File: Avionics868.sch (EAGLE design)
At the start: 65 parts, among them SW1 B3U-1000P-2P-SMD, U1 ATSAMD21G18_QFN, U2 SPX3819M5-L-3-0, U3 MCP73831T-2ACI/OT, U4 MPU-9250, U5 SIM868, U6 BMP180, X1 JSTPH, X2 32.768, X3 microUSB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

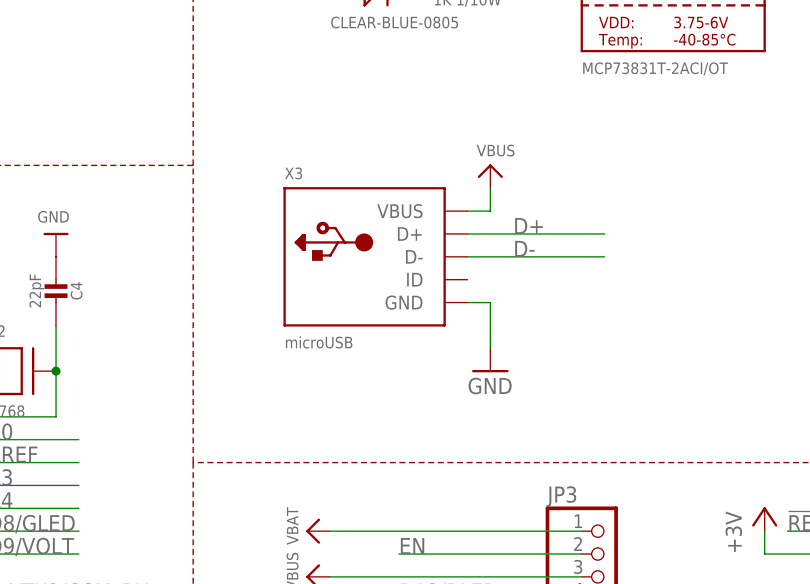
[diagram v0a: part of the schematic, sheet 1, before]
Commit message: Swapped Micro-USB connector for Seeed
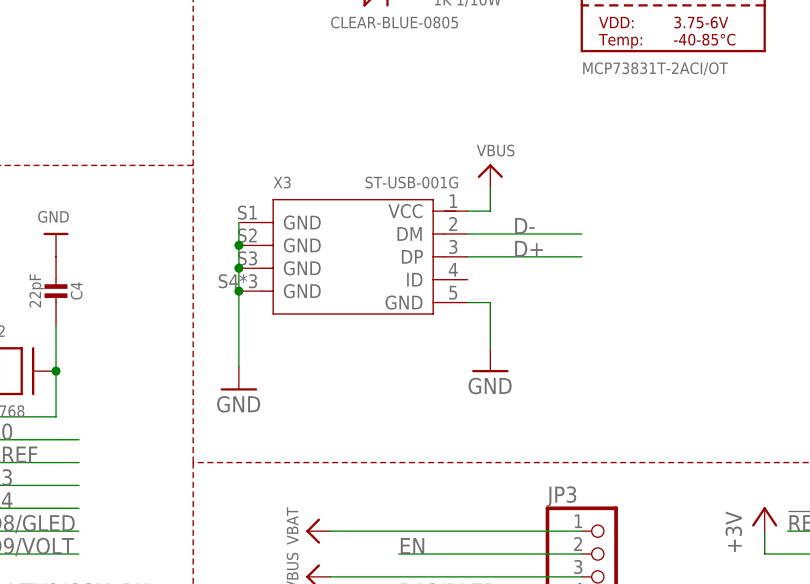
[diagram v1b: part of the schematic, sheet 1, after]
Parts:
- X3: value microUSB -> ST-USB-001G; device microbuilder:USB_MICRO_20329_V2 -> Seeed-Connector -2016:MICRO-USB-SMD-B-WITHOUT-POST-W/P(ST-USB-001G)
- renumbered X6 to X4
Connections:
- net D+: now also X3.DP; no longer X3.D+
- net D-: now also X3.DM; no longer X3.D-
- net GND: now also X3.GND@1, X3.GND@2, X3.GND@3, X3.GND@4, X3.GND@5; no longer X3.GND
- net VBUS: now also X3.VCC; no longer X3.VBUS
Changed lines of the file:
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@@
 <part name="U$3" library="microbuilder" deviceset="VBUS" device=""/>
 <part name="U$21" library="microbuilder" deviceset="VBAT" device=""/>
-<part name="X3" library="microbuilder" deviceset="USB" device="_MICRO_20329_V2" value="microUSB"/>
 <part name="U2" library="microbuilder" deviceset="VREG_SOT23-5" device="" value="SPX3819M5-L-3-0"/>
 <part name="D1" library="microbuilder" deviceset="DIODE-SCHOTTKY" device="SOD-123" value="MBR120"/>
@@
 <part name="U$47" library="microbuilder" deviceset="VBAT" device=""/>
 <part name="TP13" library="microbuilder" deviceset="TESTPOINT" device="ROUND1.5MM"/>
-<part name="X6" library="SimSdCombo" deviceset="MOLEX-SD+SIM-104239" device="" value="VSHO-21-3301"/>
+<part name="X4" library="SimSdCombo" deviceset="MOLEX-SD+SIM-104239" device="" value="VSHO-21-3301"/>
 <part name="U$4" library="microbuilder" deviceset="GND" device=""/>
 <part name="+3V11" library="Custom" deviceset="+3V" device=""/>
@@
 <part name="U$51" library="microbuilder" deviceset="GND" device=""/>
 <part name="SW1" library="Seeed-Switch-2016" deviceset="SMD-BUTTON(2P-3.0X2.5X1.2+0.4MM)" device="-B3U-1000P-2P-SMD" value="B3U-1000P-2P-SMD"/>
+<part name="X3" library="Seeed-Connector -2016" deviceset="MICRO-USB-SMD-B-WITHOUT-POST-W/P(ST-USB-001G)" device="" value="ST-USB-001G"/>
+<part name="GND2" library="supply1" deviceset="GND" device=""/>
 </parts>
 <sheets>
@@
 <instance part="U$3" gate="G$1" x="7.62" y="160.02"/>
 <instance part="U$21" gate="G$1" x="12.7" y="160.02"/>
-<instance part="X3" gate="G$1" x="154.94" y="111.76"/>
 <instance part="U2" gate="G$1" x="38.1" y="144.78"/>
 <instance part="D1" gate="G$1" x="12.7" y="154.94" rot="R270"/>
@@
 <attribute name="VALUE" x="113.538" y="160.274" size="1.27" layer="96" ratio="10"/>
 </instance>
+<instance part="X3" gate="USB" x="152.4" y="111.76"/>
+<instance part="GND2" gate="1" x="139.7" y="97.028"/>
 </instances>
 <busses>
@@
 <wire x1="167.64" y1="106.68" x2="167.64" y2="101.6" width="0.1524" layer="91"/>
 <pinref part="GND1" gate="1" pin="GND"/>
-<pinref part="X3" gate="G$1" pin="GND"/>
+<pinref part="X3" gate="USB" pin="GND@5"/>
 </segment>
 <segment>
@@
 <pinref part="GND9" gate="1" pin="GND"/>
 <wire x1="236.22" y1="46.99" x2="236.22" y2="45.72" width="0.1524" layer="91"/>
+</segment>
+<segment>
+<pinref part="X3" gate="USB" pin="GND@1"/>
+<wire x1="139.7" y1="115.57" x2="139.7" y2="113.03" width="0.1524" layer="91"/>
+<pinref part="GND2" gate="1" pin="GND"/>
+<pinref part="X3" gate="USB" pin="GND@2"/>
+<junction x="139.7" y="113.03"/>
+<wire x1="139.7" y1="113.03" x2="139.7" y2="110.49" width="0.1524" layer="91"/>
+<pinref part="X3" gate="USB" pin="GND@3"/>
+<junction x="139.7" y="110.49"/>
+<wire x1="139.7" y1="110.49" x2="139.7" y2="107.95" width="0.1524" layer="91"/>
+<pinref part="X3" gate="USB" pin="GND@4"/>
+<junction x="139.7" y="107.95"/>
+<wire x1="139.7" y1="107.95" x2="139.7" y2="99.568" width="0.1524" layer="91"/>
 </segment>
 </net>
@@
 <wire x1="167.64" y1="116.84" x2="167.64" y2="119.38" width="0.1524" layer="91"/>
 <pinref part="U$1" gate="G$1" pin="VBUS"/>
-<pinref part="X3" gate="G$1" pin="VBUS"/>
+<pinref part="X3" gate="USB" pin="VCC"/>
 </segment>
 <segment>
@@
 <net name="D+" class="0">
 <segment>
-<pinref part="X3" gate="G$1" pin="D+"/>
-<wire x1="165.1" y1="114.3" x2="180.34" y2="114.3" width="0.1524" layer="91"/>
-<label x="170.18" y="114.3" size="1.778" layer="95"/>
+<wire x1="165.1" y1="111.76" x2="177.8" y2="111.76" width="0.1524" layer="91"/>
+<label x="170.18" y="111.76" size="1.778" layer="95"/>
+<pinref part="X3" gate="USB" pin="DP"/>
 </segment>
 <segment>
@@
 <net name="D-" class="0">
 <segment>
-<pinref part="X3" gate="G$1" pin="D-"/>
-<wire x1="180.34" y1="111.76" x2="165.1" y2="111.76" width="0.1524" layer="91"/>
-<label x="170.18" y="111.76" size="1.778" layer="95"/>
+<wire x1="177.8" y1="114.3" x2="165.1" y2="114.3" width="0.1524" layer="91"/>
+<label x="170.18" y="114.3" size="1.778" layer="95"/>
+<pinref part="X3" gate="USB" pin="DM"/>
 </segment>
 <segment>
@@
 <attribute name="VALUE" x="134.112" y="98.171" size="1.27" layer="95" rot="R180" align="center-left"/>
 </instance>
-<instance part="X6" gate="G$1" x="106.68" y="86.36"/>
+<instance part="X4" gate="G$1" x="106.68" y="86.36"/>
 <instance part="U$4" gate="G$1" x="68.58" y="86.36" smashed="yes">
 <attribute name="VALUE" x="64.516" y="87.63" size="1.27" layer="96"/>
@@
 </segment>
 <segment>
-<pinref part="X6" gate="G$1" pin="GND@8"/>
-<pinref part="X6" gate="G$1" pin="GND@1"/>
+<pinref part="X4" gate="G$1" pin="GND@8"/>
+<pinref part="X4" gate="G$1" pin="GND@1"/>
 <wire x1="114.3" y1="68.58" x2="111.76" y2="68.58" width="0.1524" layer="91"/>
-<pinref part="X6" gate="G$1" pin="GND@2"/>
+<pinref part="X4" gate="G$1" pin="GND@2"/>
 <junction x="99.06" y="68.58"/>
 <wire x1="111.76" y1="68.58" x2="109.22" y2="68.58" width="0.1524" layer="91"/>
@@
 <wire x1="101.6" y1="68.58" x2="99.06" y2="68.58" width="0.1524" layer="91"/>
 <wire x1="99.06" y1="68.58" x2="96.52" y2="68.58" width="0.1524" layer="91"/>
-<pinref part="X6" gate="G$1" pin="GND@3"/>
+<pinref part="X4" gate="G$1" pin="GND@3"/>
 <junction x="101.6" y="68.58"/>
-<pinref part="X6" gate="G$1" pin="GND@4"/>
+<pinref part="X4" gate="G$1" pin="GND@4"/>
 <junction x="104.14" y="68.58"/>
-<pinref part="X6" gate="G$1" pin="GND@5"/>
+<pinref part="X4" gate="G$1" pin="GND@5"/>
 <junction x="106.68" y="68.58"/>
-<pinref part="X6" gate="G$1" pin="GND@6"/>
+<pinref part="X4" gate="G$1" pin="GND@6"/>
 <junction x="109.22" y="68.58"/>
-<pinref part="X6" gate="G$1" pin="GND@7"/>
+<pinref part="X4" gate="G$1" pin="GND@7"/>
 <junction x="111.76" y="68.58"/>
 <pinref part="U$43" gate="G$1" pin="GND"/>
@@
 </segment>
 <segment>
-<pinref part="X6" gate="G$1" pin="SIM_GND"/>
+<pinref part="X4" gate="G$1" pin="SIM_GND"/>
 <pinref part="U$48" gate="G$1" pin="GND"/>
 <wire x1="119.38" y1="111.76" x2="119.38" y2="119.38" width="0.1524" layer="91"/>
@@
 </segment>
 <segment>
-<pinref part="X6" gate="G$1" pin="SD_VSS"/>
+<pinref part="X4" gate="G$1" pin="SD_VSS"/>
 <pinref part="U$4" gate="G$1" pin="GND"/>
 <wire x1="91.44" y1="91.44" x2="68.58" y2="91.44" width="0.1524" layer="91"/>
@@
 </segment>
 <segment>
-<pinref part="X6" gate="G$1" pin="SD_VDD"/>
+<pinref part="X4" gate="G$1" pin="SD_VDD"/>
 <pinref part="+3V11" gate="G$1" pin="+3V"/>
 <wire x1="91.44" y1="96.52" x2="68.58" y2="96.52" width="0.1524" layer="91"/>
@@
 </segment>
 <segment>
-<pinref part="X6" gate="G$1" pin="SIM_VCC"/>
+<pinref part="X4" gate="G$1" pin="SIM_VCC"/>
 <wire x1="111.76" y1="111.76" x2="111.76" y2="114.3" width="0.1524" layer="91"/>
 <wire x1="111.76" y1="114.3" x2="93.98" y2="114.3" width="0.1524" layer="91"/>
@@
 </segment>
 <segment>
-<pinref part="X6" gate="G$1" pin="SIM_I/O"/>
+<pinref part="X4" gate="G$1" pin="SIM_I/O"/>
 <wire x1="124.46" y1="111.76" x2="124.46" y2="121.92" width="0.1524" layer="91"/>
 <wire x1="124.46" y1="121.92" x2="93.98" y2="121.92" width="0.1524" layer="91"/>
@@
 </segment>
 <segment>
-<pinref part="X6" gate="G$1" pin="SIM_CLK"/>
+<pinref part="X4" gate="G$1" pin="SIM_CLK"/>
 <wire x1="116.84" y1="111.76" x2="116.84" y2="119.38" width="0.1524" layer="91"/>
 <wire x1="116.84" y1="119.38" x2="93.98" y2="119.38" width="0.1524" layer="91"/>
@@
 </segment>
 <segment>
-<pinref part="X6" gate="G$1" pin="SIM_RST"/>
+<pinref part="X4" gate="G$1" pin="SIM_RST"/>
 <wire x1="114.3" y1="111.76" x2="114.3" y2="116.84" width="0.1524" layer="91"/>
 <wire x1="114.3" y1="116.84" x2="93.98" y2="116.84" width="0.1524" layer="91"/>
@@
 <net name="MOSI" class="0">
 <segment>
-<pinref part="X6" gate="G$1" pin="SD_CMD"/>
+<pinref part="X4" gate="G$1" pin="SD_CMD"/>
 <wire x1="91.44" y1="99.06" x2="73.66" y2="99.06" width="0.1524" layer="91"/>
 <label x="73.66" y="99.06" size="1.778" layer="95"/>
@@
 <net name="SCK" class="0">
 <segment>
-<pinref part="X6" gate="G$1" pin="SD_CLK"/>
+<pinref part="X4" gate="G$1" pin="SD_CLK"/>
 <wire x1="91.44" y1="93.98" x2="73.66" y2="93.98" width="0.1524" layer="91"/>
 <label x="73.66" y="93.98" size="1.778" layer="95"/>
@@
 <net name="D7/SD_CS" class="0">
 <segment>
-<pinref part="X6" gate="G$1" pin="SD_CD/DAT3"/>
+<pinref part="X4" gate="G$1" pin="SD_CD/DAT3"/>
 <wire x1="91.44" y1="101.6" x2="73.66" y2="101.6" width="0.1524" layer="91"/>
 <label x="73.66" y="101.6" size="1.778" layer="95"/>
@@
 <net name="MISO" class="0">
 <segment>
-<pinref part="X6" gate="G$1" pin="SD_DAT0"/>
+<pinref part="X4" gate="G$1" pin="SD_DAT0"/>
 <wire x1="91.44" y1="88.9" x2="73.66" y2="88.9" width="0.1524" layer="91"/>
 <label x="73.66" y="88.9" size="1.778" layer="95"/>
@@
 <net name="SD_DET" class="0">
 <segment>
-<pinref part="X6" gate="G$1" pin="SD_SWITCH"/>
+<pinref part="X4" gate="G$1" pin="SD_SWITCH"/>
 <wire x1="91.44" y1="83.82" x2="73.66" y2="83.82" width="0.1524" layer="91"/>
 <pinref part="TP3" gate="G$1" pin="P$1"/>

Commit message: Swapped some capacitors
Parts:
- C3, C5: value 10uF -> 10uf; device microbuilder:CAP_CERAMIC0805-NOOUTLINE -> Seeed-Capacitor-2016:CERAMIC-10UF-10V-10%-X5R(0603)
- X4: value VSHO-21-3301 -> 104239-1430
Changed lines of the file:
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@@
 <part name="L3" library="Seeed-LED-2016" deviceset="SMD-LED-CLEAR-BLUE(0805)" device="" value="CLEAR-BLUE-0805"/>
 <part name="R2" library="Seeed-Resistor-2016" deviceset="SMD-RES-1K-5%-1/10W(0603)" device="" value="1K 1/10W"/>
-<part name="C3" library="microbuilder" deviceset="CAP_CERAMIC" device="0805-NOOUTLINE" value="10uF"/>
+<part name="C3" library="Seeed-Capacitor-2016" deviceset="CERAMIC-10UF-10V-10%-X5R(0603)" device="" value="10uf"/>
 <part name="U$33" library="microbuilder" deviceset="GND" device=""/>
 <part name="R8" library="Seeed-Resistor-2016" deviceset="SMD-RES-10K-5%-1/10W(0603)" device="" value="10K 1/10W"/>
@@
 <part name="U$10" library="microbuilder" deviceset="GND" device=""/>
 <part name="X2" library="adafruit2" deviceset="XTAL" device="-3.2X1.5" value="32.768"/>
-<part name="C5" library="microbuilder" deviceset="CAP_CERAMIC" device="0805-NOOUTLINE" value="10uF"/>
+<part name="C5" library="Seeed-Capacitor-2016" deviceset="CERAMIC-10UF-10V-10%-X5R(0603)" device="" value="10uf"/>
 <part name="+3V2" library="Custom" deviceset="+3V" device=""/>
 <part name="U$11" library="microbuilder" deviceset="GND" device=""/>
@@
 <part name="U$47" library="microbuilder" deviceset="VBAT" device=""/>
 <part name="TP13" library="microbuilder" deviceset="TESTPOINT" device="ROUND1.5MM"/>
-<part name="X4" library="SimSdCombo" deviceset="MOLEX-SD+SIM-104239" device="" value="VSHO-21-3301"/>
+<part name="X4" library="SimSdCombo" deviceset="MOLEX-SD+SIM-104239" device="" value="104239-1430"/>
 <part name="U$4" library="microbuilder" deviceset="GND" device=""/>
 <part name="+3V11" library="Custom" deviceset="+3V" device=""/>
@@
 <instance part="L3" gate="G$1" x="154.94" y="142.24"/>
 <instance part="R2" gate="G$1" x="165.1" y="142.24"/>
-<instance part="C3" gate="G$1" x="220.98" y="139.7"/>
+<instance part="C3" gate="G$1" x="220.98" y="139.7" rot="R270"/>
 <instance part="U$33" gate="G$1" x="220.98" y="129.54"/>
 <instance part="R8" gate="G$1" x="210.82" y="144.78"/>
@@
 <instance part="U$10" gate="G$1" x="119.38" y="114.3" rot="R180"/>
 <instance part="X2" gate="G$1" x="114.3" y="99.06"/>
-<instance part="C5" gate="G$1" x="93.98" y="137.16"/>
+<instance part="C5" gate="G$1" x="93.98" y="139.7" rot="R270"/>
 <instance part="+3V2" gate="G$1" x="93.98" y="152.4" rot="MR0"/>
 <instance part="U$11" gate="G$1" x="93.98" y="127"/>
@@
 <pinref part="C3" gate="G$1" pin="2"/>
 <pinref part="U$33" gate="G$1" pin="GND"/>
-<wire x1="220.98" y1="137.16" x2="220.98" y2="132.08" width="0.1524" layer="91"/>
+<wire x1="220.98" y1="135.89" x2="220.98" y2="132.08" width="0.1524" layer="91"/>
 </segment>
 <segment>
@@
 <pinref part="C5" gate="G$1" pin="2"/>
 <pinref part="U$11" gate="G$1" pin="GND"/>
-<wire x1="93.98" y1="129.54" x2="93.98" y2="134.62" width="0.1524" layer="91"/>
+<wire x1="93.98" y1="129.54" x2="93.98" y2="135.89" width="0.1524" layer="91"/>
 </segment>
 <segment>
@@
 <pinref part="C5" gate="G$1" pin="1"/>
 <pinref part="+3V2" gate="G$1" pin="+3V"/>
-<wire x1="93.98" y1="142.24" x2="93.98" y2="149.86" width="0.1524" layer="91"/>
+<wire x1="93.98" y1="143.51" x2="93.98" y2="149.86" width="0.1524" layer="91"/>
 </segment>
 </net>
@@
 <pinref part="C3" gate="G$1" pin="1"/>
 <wire x1="220.98" y1="147.32" x2="200.66" y2="147.32" width="0.1524" layer="91"/>
-<wire x1="220.98" y1="144.78" x2="220.98" y2="147.32" width="0.1524" layer="91"/>
+<wire x1="220.98" y1="143.51" x2="220.98" y2="147.32" width="0.1524" layer="91"/>
 <wire x1="220.98" y1="147.32" x2="228.6" y2="147.32" width="0.1524" layer="91"/>
 <junction x="220.98" y="147.32"/>
@@
 <attribute name="VALUE" x="134.112" y="98.171" size="1.27" layer="95" rot="R180" align="center-left"/>
 </instance>
-<instance part="X4" gate="G$1" x="106.68" y="86.36"/>
+<instance part="X4" gate="G$1" x="106.68" y="86.36" smashed="yes">
+<attribute name="NAME" x="93.98" y="110.49" size="1.27" layer="95" ratio="10"/>
+<attribute name="VALUE" x="125.984" y="72.136" size="1.27" layer="96" ratio="10" rot="R90"/>
+</instance>
 <instance part="U$4" gate="G$1" x="68.58" y="86.36" smashed="yes">
 <attribute name="VALUE" x="64.516" y="87.63" size="1.27" layer="96"/>
